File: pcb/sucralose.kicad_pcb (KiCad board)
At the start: 2 copper layers, 153 x 89.9 mm, 96 parts, among them M1 MountingHole_1.2mm_M1

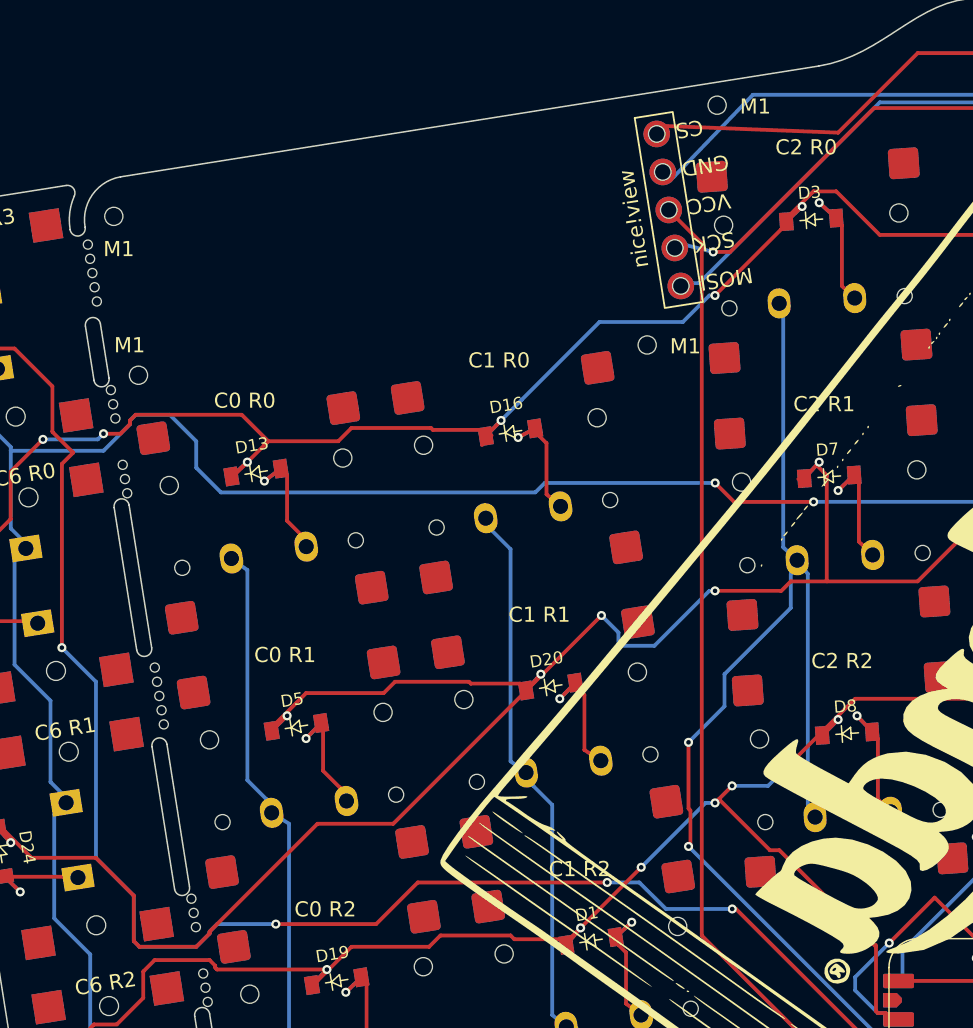
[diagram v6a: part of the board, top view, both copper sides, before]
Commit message: Display pulled back: 2.0 mm inboard of e218826 (was 2.8). Clears C2 R0 courtyard (keycap) by 0.26 mm; header pads 0.82 mm. Left display M1 holes 0.3 mm further inboard (u 56.16/56.19) to keep their 2.2 mm head courtyards off the MB1/MB2 mouse-bite NPTHs. Edge/pinky strip unchanged at 2.4 mm. DRC 361, same categories and same 7 unconnected pads.
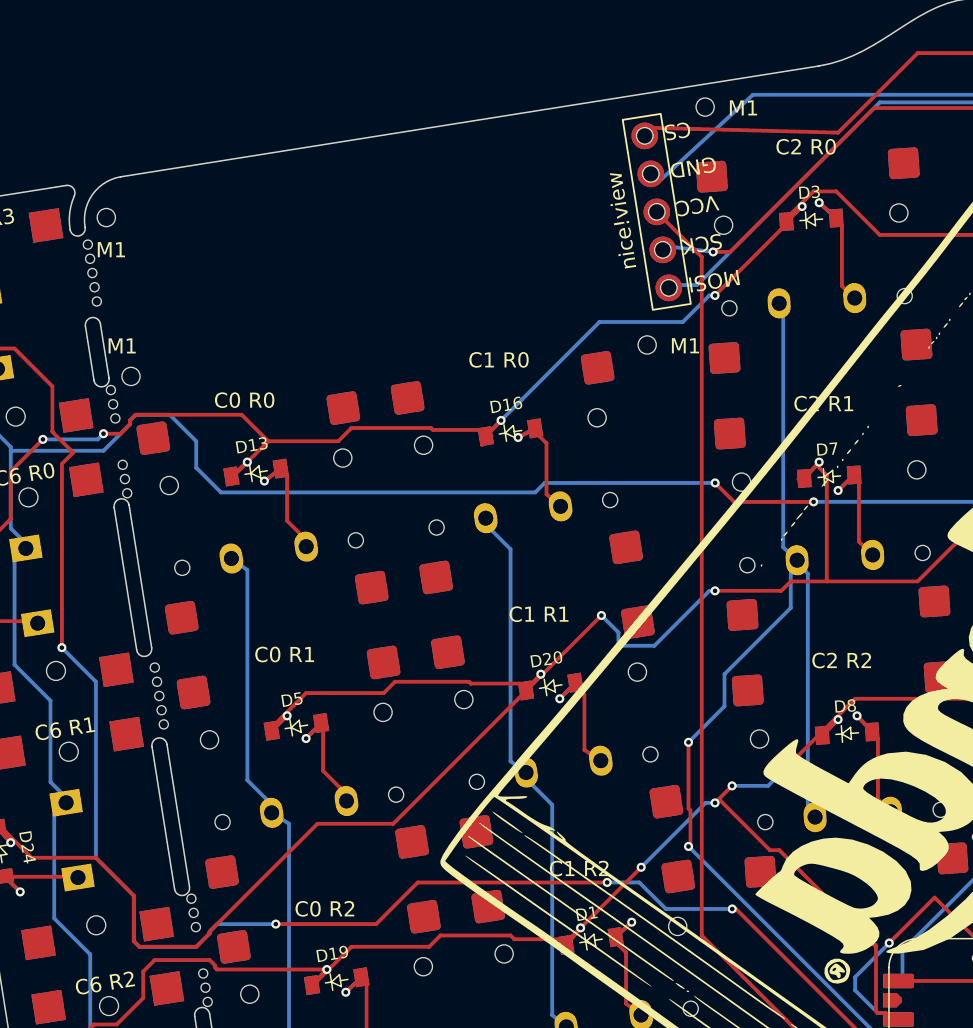
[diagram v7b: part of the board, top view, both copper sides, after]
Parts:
- moved M1 0.80 mm to (106.5, 56.2)
- moved display* 0.80 mm to (87.0, 65.7) (x2)
- moved M1 0.50 mm to (66.9, 63.5)
- moved M1 0.50 mm to (68.6, 74.0)
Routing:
- net DISP_H1: track 64.3 -> 65.2 mm
- net DISP_H5: track 63.5 -> 64.3 mm
- net DISP_H2: track 58.1 -> 58.8 mm
- net DISP_H4: track 57.4 -> 58.1 mm
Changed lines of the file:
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@@
 	(footprint "nice_view:nice_view"
 		(layer "F.Cu")
-		(at 87.765527 65.561983 99)
+		(at 86.975377 65.687131 99)
 		(property "Reference" "display*"
 			(at 0 1.27 99)
@@
 	(footprint "CustomParts:MountingHole_1.2mm_M1"
 		(layer "F.Cu")
-		(at 107.265527 56.061983)
+		(at 106.475377 56.187131)
 		(descr "Mounting Hole 1.2mm, M1, no annular. Courtyard and head outline 2.2 mm dia (ISO 7045 / JIS B 1111 M1-M1.2 pan head dk max 2.0)")
 		(tags "mountinghole M2")
@@
 	(footprint "CustomParts:MountingHole_1.2mm_M1"
 		(layer "F.Cu")
-		(at 69.064633 73.890883)
+		(at 68.57079 73.969101)
 		(descr "Mounting Hole 1.2mm, M1, no annular. Courtyard and head outline 2.2 mm dia (ISO 7045 / JIS B 1111 M1-M1.2 pan head dk max 2.0)")
 		(tags "mountinghole M2")
@@
 	(footprint "CustomParts:MountingHole_1.2mm_M1"
 		(layer "F.Cu")
-		(at 67.435277 63.401907)
+		(at 66.941434 63.480125)
 		(descr "Mounting Hole 1.2mm, M1, no annular. Courtyard and head outline 2.2 mm dia (ISO 7045 / JIS B 1111 M1-M1.2 pan head dk max 2.0)")
 		(tags "mountinghole M2")
@@
 	(footprint "nice_view:nice_view"
 		(layer "B.Cu")
-		(at 87.765527 65.561983 -81)
+		(at 86.975377 65.687131 -81)
 		(property "Reference" "display*"
 			(at 0.000001 -1.27 99)
@@
 	)
 	(segment
-		(start 105.267827 65.311983)
+		(start 104.477677 65.437131)
 		(end 107.0023 65.75)
 		(width 0.25)
@@
 	)
 	(segment
-		(start 104.392827 60.811983)
+		(start 103.602677 60.937131)
 		(end 109.6273 55.375)
 		(width 0.25)
@@
 	)
 	(segment
-		(start 105.642827 67.811983)
-		(end 106.065317 67.811983)
+		(start 104.852677 67.937131)
+		(end 105.940169 67.937131)
 		(width 0.25)
 		(layer "B.Cu")
@@
 	)
 	(segment
-		(start 106.065317 67.811983)
+		(start 105.940169 67.937131)
 		(end 118.0023 55.875)
 		(width 0.25)
@@
 	)
 	(segment
-		(start 104.642827 63.561983)
-		(end 106.2523 65.171456)
+		(start 103.852677 63.687131)
+		(end 106.2523 66.086754)
 		(width 0.25)
 		(layer "F.Cu")
@@
 	)
 	(segment
-		(start 106.2523 65.171456)
+		(start 106.2523 66.086754)
 		(end 106.2523 110.875)
 		(width 0.25)
@@
 	)
 	(segment
-		(start 103.892827 57.436983)
+		(start 103.102677 57.562131)
 		(end 115.2523 57.875)
 		(width 0.25)
@@
 		(layer "B.Cu")
 		(net "COL6")
-		(uuid "ryn8d79b-67d7-4289-9f68-3021e5a18448")
+		(uuid "ryn8cdbb-04f8-42ee-b280-d241877a2af7")
 	)
 	(segment
@@
 		(layer "B.Cu")
 		(net "COL6")
-		(uuid "ryn896e9-cac4-4937-b59f-e81bb0ca9434")
+		(uuid "ryn8a250-d190-431f-93f7-c86a1e96b16e")
 	)
 	(segment
@@
 		(layer "B.Cu")
 		(net "COL6")
-		(uuid "ryn85d41-25cf-477f-83f9-09f0b758234c")
+		(uuid "ryn86d8f-4de8-4744-ad38-b14556b047bb")
 	)
 	(segment
@@
 		(layer "B.Cu")
 		(net "COL6")
-		(uuid "ryn89c38-548e-4b43-b180-76a76934e81e")
+		(uuid "ryn8d870-e3bf-4fe9-b2b2-746204d55ee4")
 	)
 	(segment
@@
 		(layer "B.Cu")
 		(net "COL6")
-		(uuid "ryn8c700-ad54-4b02-a1e3-a5548025dfd0")
+		(uuid "ryn8cf07-2e19-409f-b2a2-bb2f20883f74")
 	)
 	(segment
@@
 		(layer "B.Cu")
 		(net "COL6")
-		(uuid "ryn8a1cf-32cc-482d-9395-2ad37f824b68")
+		(uuid "ryn86084-985c-4698-a62e-ecb57672f532")
 	)
 	(segment
@@
 		(layer "B.Cu")
 		(net "COL6")
-		(uuid "ryn89516-1dce-46ae-b475-4755804ef040")
+		(uuid "ryn8f850-59b1-41b4-990b-6ca9c400069f")
 	)
 	(segment
@@
 		(layer "B.Cu")
 		(net "ROW0")
-		(uuid "ryn827ad-963c-4945-b1dc-5c21ac70dfe8")
+		(uuid "ryn86323-7318-4d36-b6af-ff1747663288")
 	)
 	(segment
@@
 		(layer "B.Cu")
 		(net "ROW0")
-		(uuid "ryn817db-4f26-4d3e-a5ac-72d9fb187d6b")
+		(uuid "ryn8549f-f485-46dc-89da-aced61a3537f")
 	)
 	(segment
@@
 		(layer "F.Cu")
 		(net "ROW0")
-		(uuid "ryn8bc8e-5179-418e-8771-2a6085b38637")
+		(uuid "ryn87657-a9de-48eb-937a-e34b350785c6")
 	)
 	(segment
@@
 		(layer "F.Cu")
 		(net "ROW0")
-		(uuid "ryn8b0dc-e00d-49f4-ab39-17372514bf03")
+		(uuid "ryn8950d-c242-4d0f-aa0c-7da9b9e24318")
 	)
 	(segment
@@
 		(layer "F.Cu")
 		(net "ROW0")
-		(uuid "ryn80ef7-5683-4181-8f1c-93dba292289a")
+		(uuid "ryn8c8c7-fbec-46b0-9da8-2c55b9505049")
 	)
 	(segment
@@
 		(layer "F.Cu")
 		(net "ROW0")
-		(uuid "ryn8631e-6a93-44c3-81df-ff1eebe8bb08")
+		(uuid "ryn86135-45e5-4547-a9d5-00b18649836a")
 	)
 	(segment
@@
 		(layer "F.Cu")
 		(net "ROW0")
-		(uuid "ryn86217-fed8-4880-9f94-80062a8823ee")
+		(uuid "ryn8f290-d8d2-4394-a6de-13db0ecc3c4b")
 	)
 	(segment
@@
 		(layer "F.Cu")
 		(net "ROW0")
-		(uuid "ryn8e92d-b0fc-4797-a958-6d86ae8bcd96")
+		(uuid "ryn82700-cfe4-4015-a346-dba64c67eb2a")
 	)
 	(segment
@@
 		(layer "F.Cu")
 		(net "ROW1")
-		(uuid "ryn890f2-4ada-4117-9851-c2cdad777ef4")
+		(uuid "ryn885d2-cf05-4ed6-9de7-6d3517a05a99")
 	)
 	(segment
@@
 		(layer "F.Cu")
 		(net "ROW1")
-		(uuid "ryn829f9-e206-4cd6-b02e-1b3ec2e97112")
+		(uuid "ryn80122-887a-4130-883d-f2c62c3936e3")
 	)
 	(segment
@@
 		(layer "F.Cu")
 		(net "ROW1")
-		(uuid "ryn84e6a-26d1-4542-87df-6e50365af9a3")
+		(uuid "ryn861fe-76b7-482c-a95c-d8753eab983b")
 	)
 	(segment
@@
 		(layer "F.Cu")
 		(net "ROW1")
-		(uuid "ryn89e99-e05e-47b3-9bbe-db9f24ab2bb8")
+		(uuid "ryn827ab-df33-4b37-b6fa-8f7be0810c7d")
 	)
 	(segment
@@
 		(layer "F.Cu")
 		(net "ROW2")
-		(uuid "ryn80510-bbfb-4653-ba23-8a049f48fa6a")
+		(uuid "ryn8aa1a-92d4-40f2-a980-8c4e857fcbec")
 	)
 	(segment
@@
 		(layer "F.Cu")
 		(net "ROW2")
-		(uuid "ryn82540-ab59-404b-9822-28a92e370a95")
+		(uuid "ryn80555-de96-4f77-b755-df1a91138b9f")
 	)
 	(segment
@@
 		(layer "F.Cu")
 		(net "ROW2")
-		(uuid "ryn83da1-0bc7-43be-b046-7a04c98ee18e")
+		(uuid "ryn82628-8f71-4475-95c5-78300ab03d21")
 	)
 	(segment
@@
 		(layer "F.Cu")
 		(net "ROW2")
-		(uuid "ryn8e0ce-ef7e-43e2-bece-1137940b812b")
+		(uuid "ryn82f95-f022-4075-8891-589094d9cd8c")
 	)
 	(segment
@@
 		(layer "F.Cu")
 		(net "ROW2")
-		(uuid "ryn82d23-b971-402d-8b16-f3e656bfeb66")
+		(uuid "ryn8630a-687d-4865-900e-ba8eb918adf8")
 	)
 	(segment
@@
 		(layer "F.Cu")
 		(net "ROW3")
-		(uuid "ryn81fea-4d33-40b2-818b-4193365c0581")
+		(uuid "ryn896a8-04b0-49c3-b623-3f7065f86bda")
 	)
 	(segment
@@
 		(layer "F.Cu")
 		(net "ROW3")
-		(uuid "ryn85671-8cd7-4012-afaa-9f93d5a373c3")
+		(uuid "ryn87810-28cd-49bb-9f6d-0bd9fce2cc12")
 	)
 	(segment
@@
 		(layer "B.Cu")
 		(net "ROW3")
-		(uuid "ryn84d42-9ec5-4e9e-90ba-c211bfc16d64")
+		(uuid "ryn8c2aa-4355-4e94-ab13-8ce3921584f6")
 	)
 	(segment
@@
 		(layer "B.Cu")
 		(net "ROW3")
-		(uuid "ryn8ed02-02ba-4012-bd72-b30dc0359c19")
+		(uuid "ryn866a7-fa87-4152-96bb-2e44d6448505")
 	)
 	(segment
@@
 		(layer "B.Cu")
 		(net "ROW3")
-		(uuid "ryn8ab79-a22f-4c60-8d4c-8d07618fbbcd")
+		(uuid "ryn8752a-9818-4269-8b91-15c5646fa0df")
 	)
 	(segment
@@
 		(layer "B.Cu")
 		(net "ROW3")
-		(uuid "ryn8aaf8-25f6-4918-9465-d3246d2b9c70")
+		(uuid "ryn85220-2799-44bd-a509-9d910afb89cd")
 	)
 	(segment
@@
 		(layer "B.Cu")
 		(net "ROW3")
-		(uuid "ryn829e6-a8fa-4637-b65e-a2d773a58f79")
+		(uuid "ryn8a392-8a49-4607-b1c4-c999e2a9f99e")
 	)
 	(segment
@@
 		(layer "B.Cu")
 		(net "ROW3")
-		(uuid "ryn8d392-4783-4dd1-935f-35f43a96bde9")
+		(uuid "ryn84f94-9537-4612-8bf1-ca9aa3cc7906")
 	)
 	(segment
@@
 		(layer "B.Cu")
 		(net "ROW3")
-		(uuid "ryn86ba4-a314-42ab-891e-47d3f6ae5d8f")
+		(uuid "ryn89a83-b113-455f-b6b3-90ebc2aaeffb")
 	)
 	(segment
@@
 		(layer "B.Cu")
 		(net "ROW3")
-		(uuid "ryn8a034-a60c-4ce6-9a58-98d87b8c74ce")
+		(uuid "ryn8ec7d-a2a6-44a3-8916-8aec8014c7c9")
 	)
 	(segment
@@
 		(layer "B.Cu")
 		(net "ROW3")
-		(uuid "ryn86390-65a6-4099-9ff4-a16cd5a93ca6")
+		(uuid "ryn81364-169c-43cc-9547-1a5ed1be87df")
 	)
 	(segment
@@
 		(layer "B.Cu")
 		(net "ROW3")
-		(uuid "ryn8b560-60ef-40f1-a805-1232771df2d0")
+		(uuid "ryn8e134-c98a-41ce-ae75-3f866671f456")
 	)
 	(segment
@@
 		(layer "F.Cu")
 		(net "ROW3")
-		(uuid "ryn8d962-c8ba-4071-8cf9-92e3d02b2eda")
+		(uuid "ryn8deb4-6df3-4f47-812e-37ea43eef22c")
 	)
 	(segment
@@
 		(layer "F.Cu")
 		(net "ROW3")
-		(uuid "ryn88859-514e-4994-a750-d1ad4fbd4298")
+		(uuid "ryn87e10-7def-474d-85a9-7397f0d22574")
 	)
 	(segment
@@
 		(layer "F.Cu")
 		(net "ROW3")
-		(uuid "ryn8db19-502f-43c2-9466-282e82f8c55a")
+		(uuid "ryn80602-478b-4bed-8bc3-c42e67d11590")
 	)
 	(segment
@@
 		(layer "B.Cu")
 		(net "ROW3")
-		(uuid "ryn88abc-5b9d-4d7f-976c-dac2cb824d69")
+		(uuid "ryn850bb-7e22-453d-b456-0ef66aafef54")
 	)
 	(via
@@
 		(layers "F.Cu" "B.Cu")
 		(net "ROW0")
-		(uuid "ryn8193f-639e-4ee3-be07-8d99ce9aa2fb")
+		(uuid "ryn8bd5e-01b4-4f39-839d-619617db1525")
 	)
 	(via
@@
 		(layers "F.Cu" "B.Cu")
 		(net "ROW3")
-		(uuid "ryn83424-168a-4aaa-bd6f-e82f72862bfe")
+		(uuid "ryn867d6-bcef-4635-bd66-5b910c09c1dc")
 	)
 	(via
@@
 		(layers "F.Cu" "B.Cu")
 		(net "ROW3")
-		(uuid "ryn8f303-5e77-4214-ba86-1cf7b2b14053")
+		(uuid "ryn88607-74ac-4b17-880f-040b07642154")
 	)
 	(via
@@
 		(layers "F.Cu" "B.Cu")
 		(net "ROW3")
-		(uuid "ryn86a0d-1e86-4924-a38a-4fe685cc9a83")
+		(uuid "ryn8b02f-536a-481c-a72e-50cb884f6456")
 	)
 )

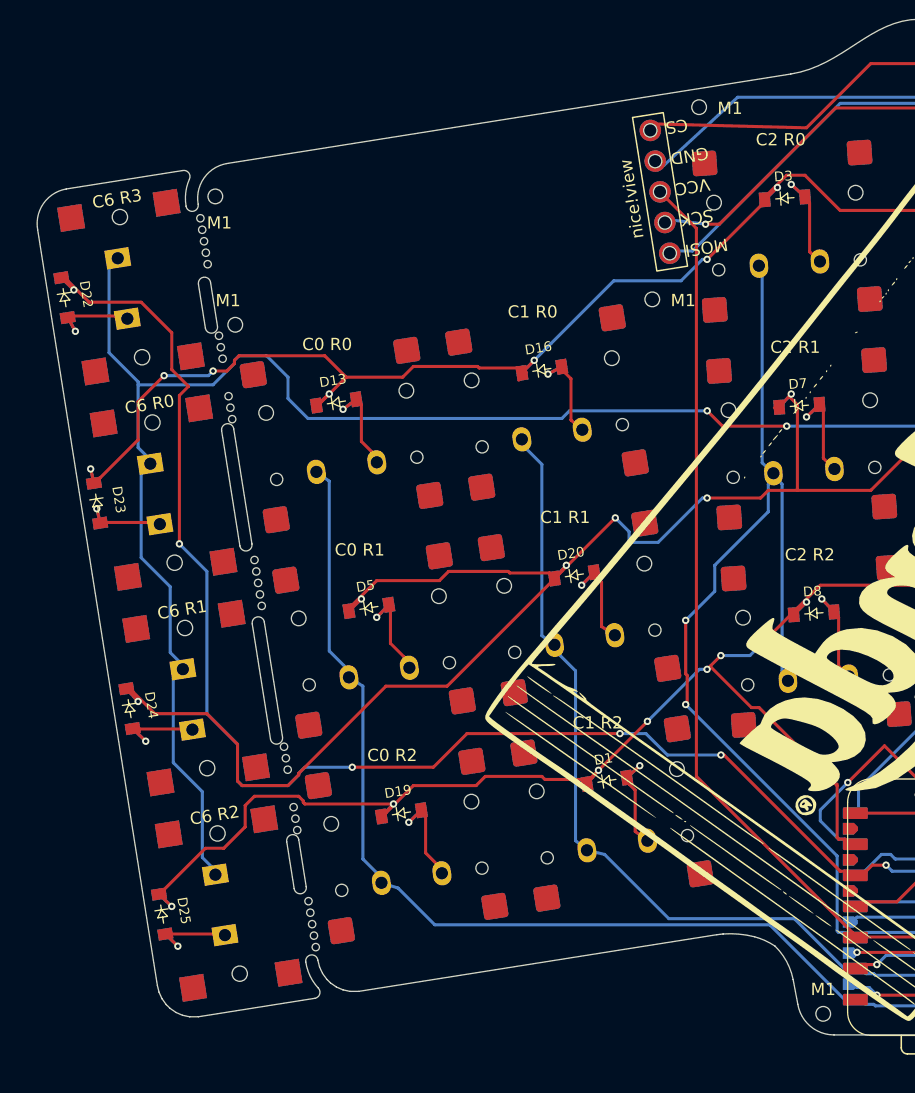
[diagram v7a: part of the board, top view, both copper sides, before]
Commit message: Display 1 mm back outboard (now 1.0 mm inboard of e218826) with its top and two left M1 holes; header M1 unchanged. Main left edge + pinky-col7 strip moved out 1 mm to match (edge u 53.70, 1.62 mm from C0 keycap); left holes keep 1.5 mm to the edge. Display clears C2 R0 courtyard by 1.26 mm. Bridge nets re-routed. DRC 361, same categories and same 7 unconnected pads.
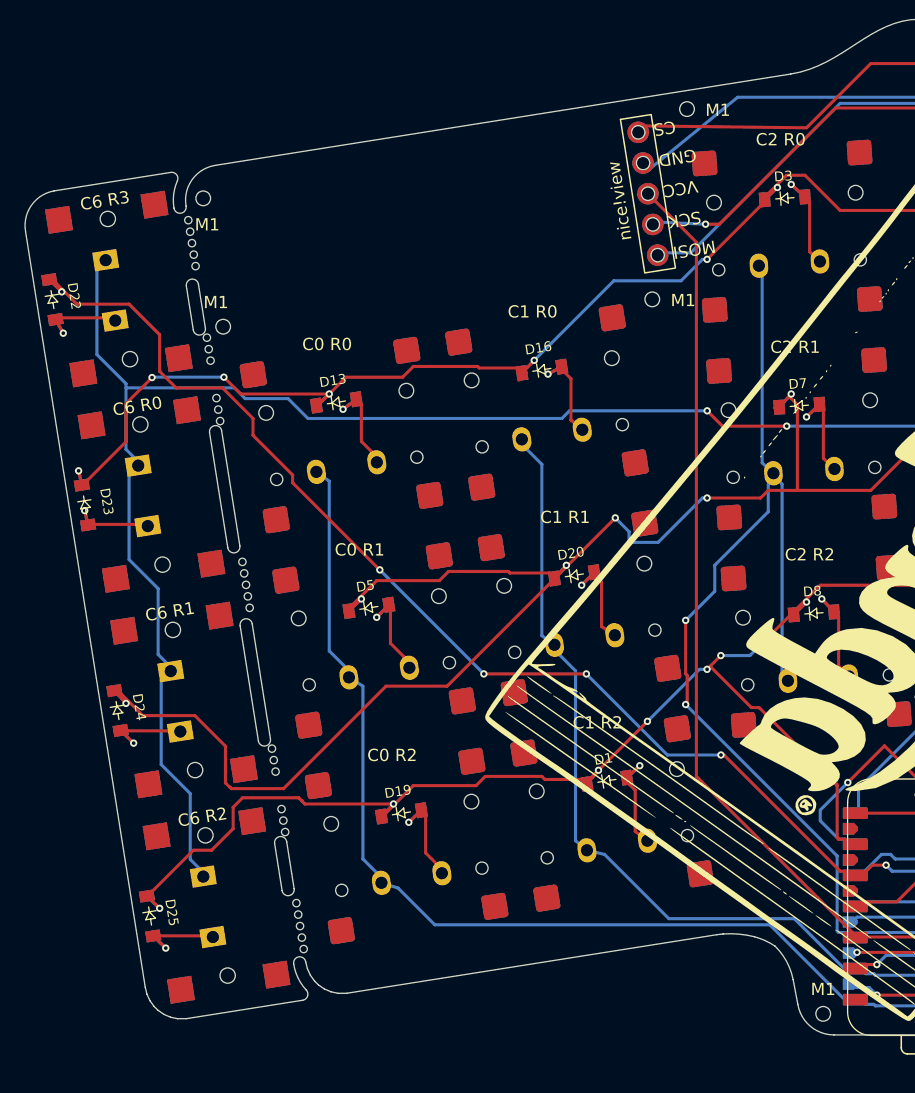
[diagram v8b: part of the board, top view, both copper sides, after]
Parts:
- moved M1 1.00 mm to (105.5, 56.3)
- moved display* 1.00 mm to (86.0, 65.8) (x2)
- moved M1 1.00 mm to (67.6, 74.1)
- moved M1 1.00 mm to (66.0, 63.6)
- moved D23 1.00 mm to (56.3, 88.7)
- moved MB2 1.00 mm to (66.8, 78.4)
- moved MB3 1.00 mm to (72.1, 112.0)
- moved MB4 1.00 mm to (73.9, 123.1)
- moved C6 R0 1.00 mm to (61.7, 87.8)
- moved D22 1.00 mm to (53.6, 71.9)
- moved D24 1.00 mm to (59.0, 105.5)
- moved C6 R3 1.00 mm to (59.1, 71.0)
- moved D25 1.00 mm to (61.6, 122.3)
- moved C6 R1 1.00 mm to (64.4, 104.6)
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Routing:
- net ROW3: track 193.1 -> 174.5 mm
- net COL6: track 219.6 -> 217.4 mm
- net ROW0: track 243.2 -> 241.9 mm
- net ROW1: track 235.9 -> 236.9 mm
- net DISP_H1: track 65.2 -> 66.2 mm
- net DISP_H5: track 64.3 -> 65.3 mm
- net DISP_H2: track 58.8 -> 59.8 mm
- net ROW2: track 189.8 -> 190.6 mm
- net DISP_H4: track 58.1 -> 58.9 mm
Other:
- board size 153 x 89.9 mm -> 154 x 89.9 mm
